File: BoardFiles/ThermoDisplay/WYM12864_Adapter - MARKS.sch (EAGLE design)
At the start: 6 parts, among them J1 JMP_3WAY, U1 PCA8575DSOIC-24

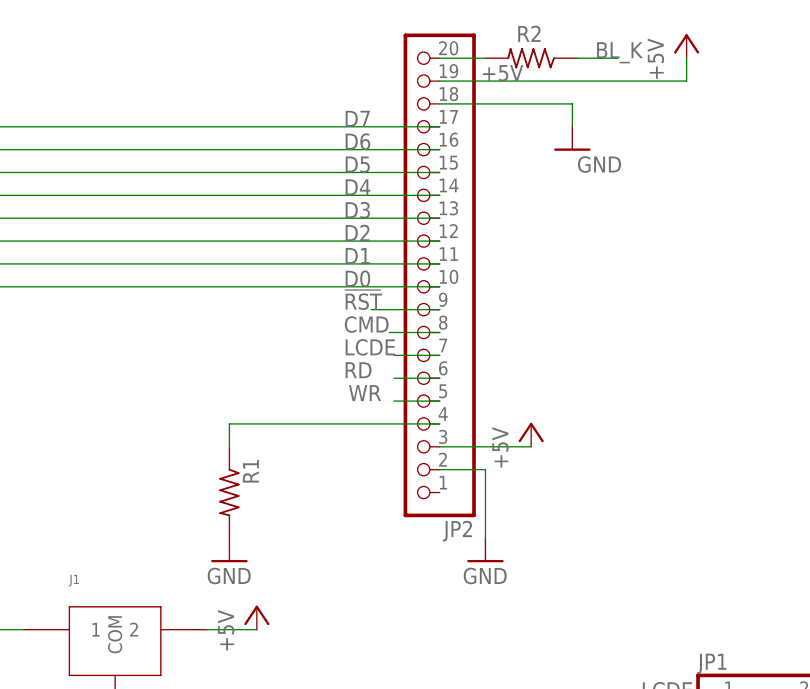
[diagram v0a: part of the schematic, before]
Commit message: Fixed board schematic/board errors
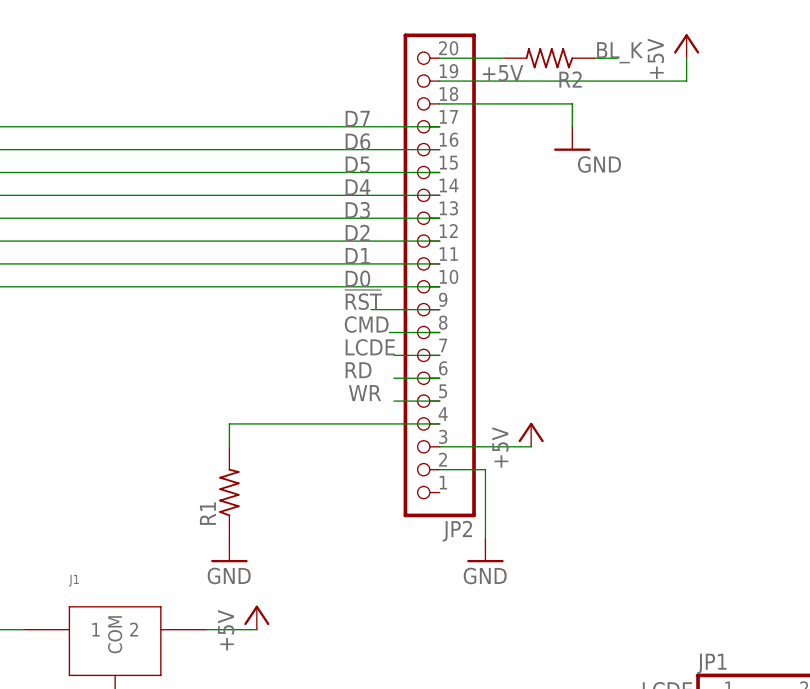
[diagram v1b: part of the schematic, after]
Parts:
- R1, R2: device rcl:R-US_M1206 -> DR:R-US_M0805
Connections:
- net GND: now also R1.1; no longer R1.2
- net N$2: now also R1.2; no longer R1.1
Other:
- moved on the sheet: R1, R2
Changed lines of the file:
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@@
 <?xml version="1.0" encoding="utf-8"?>
 <!DOCTYPE eagle SYSTEM "eagle.dtd">
-<eagle version="7.5.0">
+<eagle version="9.6.2">
 <drawing>
 <settings>
 <setting alwaysvectorfont="no"/>
+<setting keepoldvectorfont="yes"/>
 <setting verticaltext="up"/>
 </settings>
@@
 <part name="GND1" library="supply1" deviceset="GND" device=""/>
 <part name="P+1" library="supply1" deviceset="+5V" device=""/>
-<part name="R2" library="rcl" deviceset="R-US_" device="M1206"/>
 <part name="GND4" library="supply1" deviceset="GND" device=""/>
 <part name="+3V2" library="supply1" deviceset="+3V3" device=""/>
 <part name="GND5" library="supply1" deviceset="GND" device=""/>
 <part name="U1" library="DR" deviceset="PCA8575D" device="SOIC-24"/>
-<part name="JP2" library="pinhead" deviceset="PINHD-1X20" device=""/>
-<part name="JP1" library="pinhead" deviceset="PINHD-2X5" device=""/>
-<part name="R1" library="rcl" deviceset="R-US_" device="M1206"/>
+<part name="JP2" library="pinhead" library_urn="urn:adsk.eagle:library:325" deviceset="PINHD-1X20" device="" package3d_urn="urn:adsk.eagle:package:22441/2"/>
+<part name="JP1" library="pinhead" library_urn="urn:adsk.eagle:library:325" deviceset="PINHD-2X5" device="" package3d_urn="urn:adsk.eagle:package:22470/2"/>
 <part name="GND7" library="supply1" deviceset="GND" device=""/>
 <part name="GND8" library="supply1" deviceset="GND" device=""/>
@@
 <part name="GND2" library="supply1" deviceset="GND" device=""/>
 <part name="GND3" library="supply1" deviceset="GND" device=""/>
+<part name="R1" library="DR" deviceset="R-US_" device="M0805"/>
+<part name="R2" library="DR" deviceset="R-US_" device="M0805"/>
 </parts>
 <sheets>
@@
 <attribute name="VALUE" x="81.788" y="35.56" size="1.778" layer="96" rot="R90"/>
 </instance>
-<instance part="R2" gate="G$1" x="84.328" y="81.28" smashed="yes" rot="R180">
-<attribute name="NAME" x="85.598" y="84.8614" size="1.778" layer="95" rot="R180"/>
-<attribute name="VALUE" x="88.138" y="84.582" size="1.778" layer="96" rot="R180"/>
-</instance>
 <instance part="GND4" gate="1" x="10.16" y="12.7" smashed="yes">
 <attribute name="VALUE" x="7.62" y="10.16" size="1.778" layer="96"/>
@@
 <attribute name="VALUE" x="102.87" y="-5.08" size="1.778" layer="96"/>
 </instance>
-<instance part="R1" gate="G$1" x="50.8" y="33.02" smashed="yes" rot="R270">
-<attribute name="NAME" x="52.2986" y="36.83" size="1.778" layer="95" rot="R270"/>
-<attribute name="VALUE" x="47.498" y="36.83" size="1.778" layer="96" rot="R270"/>
-</instance>
 <instance part="GND7" gate="1" x="50.8" y="25.4" smashed="yes">
 <attribute name="VALUE" x="48.26" y="22.86" size="1.778" layer="96"/>
@@
 <instance part="GND3" gate="1" x="53.34" y="-7.62" smashed="yes">
 <attribute name="VALUE" x="50.8" y="-10.16" size="1.778" layer="96"/>
+</instance>
+<instance part="R1" gate="G$1" x="50.8" y="33.02" smashed="yes" rot="R90">
+<attribute name="NAME" x="49.3014" y="29.21" size="1.778" layer="95" rot="R90"/>
+<attribute name="VALUE" x="54.102" y="29.21" size="1.778" layer="96" rot="R90"/>
+</instance>
+<instance part="R2" gate="G$1" x="86.36" y="81.28" smashed="yes" rot="R180">
+<attribute name="NAME" x="90.17" y="79.7814" size="1.778" layer="95" rot="R180"/>
+<attribute name="VALUE" x="90.17" y="84.582" size="1.778" layer="96" rot="R180"/>
 </instance>
 </instances>
@@
 </segment>
 <segment>
-<pinref part="R1" gate="G$1" pin="2"/>
-<pinref part="GND7" gate="1" pin="GND"/>
-</segment>
-<segment>
 <pinref part="JP2" gate="A" pin="18"/>
 <wire x1="74.168" y1="76.2" x2="88.9" y2="76.2" width="0.1524" layer="91"/>
@@
 <wire x1="38.1" y1="-5.08" x2="53.34" y2="-5.08" width="0.1524" layer="91"/>
 </segment>
+<segment>
+<pinref part="GND7" gate="1" pin="GND"/>
+<pinref part="R1" gate="G$1" pin="1"/>
+</segment>
 </net>
 <net name="N$2" class="0">
@@
 <pinref part="JP2" gate="A" pin="4"/>
 <wire x1="74.168" y1="40.64" x2="50.8" y2="40.64" width="0.1524" layer="91"/>
-<pinref part="R1" gate="G$1" pin="1"/>
 <wire x1="50.8" y1="38.1" x2="50.8" y2="40.64" width="0.1524" layer="91"/>
+<pinref part="R1" gate="G$1" pin="2"/>
 </segment>
 </net>
@@
 <net name="N$7" class="0">
 <segment>
+<pinref part="JP2" gate="A" pin="20"/>
+<wire x1="81.28" y1="81.28" x2="74.168" y2="81.28" width="0.1524" layer="91"/>
 <pinref part="R2" gate="G$1" pin="2"/>
-<pinref part="JP2" gate="A" pin="20"/>
-<wire x1="79.248" y1="81.28" x2="74.168" y2="81.28" width="0.1524" layer="91"/>
 </segment>
 </net>
@@
 <net name="BL_K" class="0">
 <segment>
+<label x="91.44" y="81.28" size="1.778" layer="95"/>
+<wire x1="91.948" y1="81.28" x2="93.98" y2="81.28" width="0.1524" layer="91"/>
 <pinref part="R2" gate="G$1" pin="1"/>
-<wire x1="89.408" y1="81.28" x2="93.98" y2="81.28" width="0.1524" layer="91"/>
-<label x="91.44" y="81.28" size="1.778" layer="95"/>
+<wire x1="91.44" y1="81.28" x2="91.948" y2="81.28" width="0.1524" layer="91"/>
 </segment>
 <segment>
@@
 </schematic>
 </drawing>
+<compatibility>
+<note version="8.2" severity="warning">
+Since Version 8.2, EAGLE supports online libraries. The ids
+of those online libraries will not be understood (or retained)
+with this version.
+</note>
+<note version="8.3" severity="warning">
+Since Version 8.3, EAGLE supports URNs for individual library
+assets (packages, symbols, and devices). The URNs of those assets
+will not be understood (or retained) with this version.
+</note>
+<note version="8.3" severity="warning">
+Since Version 8.3, EAGLE supports the association of 3D packages
+with devices in libraries, schematics, and board files. Those 3D
+packages will not be understood (or retained) with this version.
+</note>
+</compatibility>
 </eagle>
